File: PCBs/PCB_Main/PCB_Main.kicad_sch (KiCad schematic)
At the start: 12 parts, among them J1 Conn_01x03_Pin, J10 To_Audio, J3 Light Sensor Connector, J4 USB_B_Micro, J5 LED connectors, J6 XT60-M, J7 HUB75, U8 ESP32-WROVER-E

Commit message: new
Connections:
- net at J3.2 (Pin_2): now also U8.6 (GPIO34/ADC1_CH6)
- net at J10.1 (Pin_1): now also U8.10 (DAC_1/ADC2_CH8/GPIO25)
- net at J10.2 (Pin_2): now also U8.11 (DAC_2/ADC2_CH9/GPIO26)
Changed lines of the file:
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@@
+    (stroke (width 0) (type default))
+  )
+  (wire (pts (xy 121.92 69.85) (xy 121.92 59.69))
     (stroke (width 0) (type default))
   )
@@
   )
   (wire (pts (xy 25.4 15.24) (xy 25.4 19.05))
+    (stroke (width 0) (type default))
+  )
+  (wire (pts (xy 208.28 64.77) (xy 262.89 64.77))
+    (stroke (width 0) (type default))
+  )
+  (wire (pts (xy 121.92 59.69) (xy 137.16 59.69))
+    (stroke (width 0) (type default))
+  )
+  (wire (pts (xy 101.6 69.85) (xy 121.92 69.85))
+    (stroke (width 0) (type default))
+  )
+  (wire (pts (xy 260.35 67.31) (xy 260.35 77.47))
     (stroke (width 0) (type default))
   )
@@
     (stroke (width 0) (type default))
   )
+  (wire (pts (xy 262.89 64.77) (xy 262.89 74.93))
+    (stroke (width 0) (type default))
+  )
+  (wire (pts (xy 262.89 74.93) (xy 266.7 74.93))
+    (stroke (width 0) (type default))
+  )
+  (wire (pts (xy 260.35 77.47) (xy 266.7 77.47))
+    (stroke (width 0) (type default))
+  )
   (wire (pts (xy 262.89 25.4) (xy 265.43 25.4))
     (stroke (width 0) (type default))
@@
   )
   (wire (pts (xy 262.89 43.18) (xy 262.89 49.53))
+    (stroke (width 0) (type default))
+  )
+  (wire (pts (xy 101.6 39.37) (xy 101.6 69.85))
     (stroke (width 0) (type default))
   )
@@
     (stroke (width 0) (type default))
   )
+  (wire (pts (xy 109.22 39.37) (xy 101.6 39.37))
+    (stroke (width 0) (type default))
+  )
+  (wire (pts (xy 208.28 67.31) (xy 260.35 67.31))
+    (stroke (width 0) (type default))
+  )

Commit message: updated PCB main
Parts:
- removed J10: To_Audio, Connector_JST:JST_EH_B2B-EH-A_1x02_P2.50mm_Vertical, symbol Connector_Generic:Conn_01x02
- removed J3: Light Sensor Connector, Connector_JST:JST_EH_B3B-EH-A_1x03_P2.50mm_Vertical, symbol Connector_Generic:Conn_01x03
- removed U8: ESP32-WROVER-E, PCM_Espressif:ESP32-WROVER-E, symbol PCM_Espressif:ESP32-WROVER-E
- removed VR1: 5V-3.3V LDO, Artisyn_Components:VREG_LM3940IMP-3.3_NOPB, symbol LM3940IMP-3.3_NOPB:LM3940IMP-3.3_NOPB
- added C1, C2, C8: 22uF, Capacitor_SMD:C_0805_2012Metric, symbol Device:C
- added C3: 4.7uF, Capacitor_SMD:C_0805_2012Metric, symbol Device:C
- added C4, C5, C6, C7, C9: .1uF, Capacitor_SMD:C_0805_2012Metric, symbol Device:C
- added D1: RED LED, symbol Device:LED
- added D2, D3, D4, D5: BZX84Cxx, Package_TO_SOT_SMD:SOT-23, symbol Diode:BZX84Cxx
- added J2: To_Audio, Connector_PinHeader_2.54mm:PinHeader_1x02_P2.54mm_Vertical, symbol Connector:Conn_01x02_Pin
- added LightSensorConnector1: Conn_01x03_Pin, Connector_PinHeader_2.54mm:PinHeader_1x03_P2.54mm_Vertical, symbol Connector:Conn_01x03_Pin
- added Q1, Q2: S8050, Package_TO_SOT_THT:TO-92_Inline, symbol Transistor_BJT:S8050
- added R1: 22.1k, Resistor_SMD:R_0805_2012Metric, symbol Device:R
- added R10, R5: 2k, Resistor_SMD:R_0805_2012Metric, symbol Device:R
- added R11, R12, R14: 100, Resistor_SMD:R_0805_2012Metric, symbol Device:R
- added R13, R6, R7, R8: 10k, Resistor_SMD:R_0805_2012Metric, symbol Device:R
- added R2: 47.5k, Resistor_SMD:R_0805_2012Metric, symbol Device:R
- added R4, R9: 0, Resistor_SMD:R_0805_2012Metric, symbol Device:R
- added SW1, SW2: SW_Push, symbol Switch:SW_Push
- added U1: CP2102N-Axx-xQFN28, Package_DFN_QFN:QFN-28-1EP_5x5mm_P0.5mm_EP3.35x3.35mm, symbol Interface_USB:CP2102N-Axx-xQFN28
- added U2: AMS1117-3.3, Package_TO_SOT_SMD:SOT-223-3_TabPin2, symbol Regulator_Linear:AMS1117-3.3
- added U3: ESP32-WROOM-E, PCM_Espressif:ESP32-WROOM-32E, symbol PCM_Espressif:ESP32-WROOM-E
- J1: value Conn_01x03_Pin -> LED Connectors+
- J5: value LED connectors -> LED connectors -
- J7: footprint (none) -> Connector_PinHeader_2.54mm:PinHeader_2x08_P2.54mm_Vertical
- R3, TH1: footprint (none) -> Resistor_SMD:R_0805_2012Metric
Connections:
- net GND: now also C1.2, C2.2, C3.1, C4.1, C5.1, C6.1, C7.2, C8.2, C9.2, D1.1 (K), D2.1 (A), D4.1 (A), D5.1 (A), LightSensorConnector1.1 (Pin_1), R2.2, R6.2, SW1.1, SW2.1, U1.29 (GND), U1.3 (GND), U2.1 (GND), U3.1 (GND), U3.15 (GND), U3.38 (GND), U3.39 (GND_THERMAL)
- net VCC: now also C1.1, D3.3 (K), R10.1, U2.3 (VI); no longer J4.1 (VBUS)
- net 3.3V: now reaches TH1.1
- net 3.3V: now also C2.1, C3.2, C4.2, C8.1, C9.1, LightSensorConnector1.3 (Pin_3), R13.1, R5.1, U1.6 (VDD), U1.7 (VREGIN), U2.2 (VO), U3.2 (3V3)
- net Therm_out: now reaches R3.1, TH1.2
- net at J4.2 (D-): now also R12.1
- net at J4.3 (D+): now also R11.1
- new net: R1.1, R2.1, U1.8 (VBUS)
- new net: R5.2, U1.9 (~{RST})
- new net: R6.1, U1.11 (~{SUSPEND})
- new net: Q2.2 (B), R8.2
- new net: D1.2 (A), R10.2
- new net: Q1.2 (B), R7.2
- new net: J4.1 (VBUS), R14.1
- new net: C7.1, R13.2
- new net CTS: U1.23 (~{CTS})
- new net DCD: U1.1 (~{DCD})
- new net DSR: U1.27 (~{DSR})
- new net DTR: Q2.1 (E), R7.1, U1.28 (~{DTR})
- new net EN: C6.2, Q1.3 (C), SW2.2
- new net IO0: C5.2, Q2.3 (C), SW1.2
- new net Light_Out: LightSensorConnector1.2 (Pin_2)
- new net RI: U1.2 (~{RI}/CLK)
- new net RTS: Q1.1 (E), R8.1, U1.24 (~{RTS})
- new net RXD: R9.2, U1.25 (RXD)
- new net RXD0: R4.1
- new net TXD: R4.2, U1.26 (TXD)
- new net TXD0: R9.1
- new net USB_DN: D5.3 (K), R11.2, U1.5 (D-)
- new net USB_DP: D4.3 (K), R12.2, U1.4 (D+)
- new net Vbus: D2.3 (K), D3.1 (A), R1.2, R14.2
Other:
- note added: "5V-3.3VLDO"
- note added: "Audio Signals to other board"
- note added: "Exterior Bluetooth module"
- note added: "LED CONNECTORS"
- note added: "LED Display Signals"
- note added: "MICRO USB 5V USB-UART"
- note added: "MIRCO"
- note added: "POWER ONTO BOARD"
- note added: "SENSORS"
- note added: "SWITCH BUTTIONS"
- moved on the sheet: HM19, J1, J4, J5, J6, J7, R3, TH1

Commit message: latest PCBs
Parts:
- added C10: 22uF, Capacitor_SMD:C_0805_2012Metric, symbol Device:C
- added C11, C12: .1uF, Capacitor_SMD:C_0805_2012Metric, symbol Device:C
- added R15: 10k, Resistor_SMD:R_0805_2012Metric, symbol Device:R
- added U4: PCM5102A, Package_SO:TSSOP-20_4.4x6.5mm_P0.65mm, symbol Audio:PCM5102A
- added U6: ESP32-WROVER-E, PCM_Espressif:ESP32-WROVER-E, symbol PCM_Espressif:ESP32-WROVER-E
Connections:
- net 3.3V: now also C10.1, C11.1, R15.1, U6.2 (3V3)
- net GND: now also C10.2, C11.2, C12.2, U6.1 (GND), U6.15 (GND), U6.38 (GND), U6.39 (GND_THERMAL)
- new net: C12.1, R15.2
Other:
- note added: "External DAC"
- note added: "MIRCO1 WROOM"
- note added: "MIRCO1 WROVER"
- note removed: "MIRCO"

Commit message: PCB combination
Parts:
- removed J2: To_Audio, Connector_PinHeader_2.54mm:PinHeader_1x02_P2.54mm_Vertical, symbol Connector:Conn_01x02_Pin
- added C0L1, C0R1, C3b1: 1000uF, Artisyn_Components:Audio_1000uF, symbol Device:C_Polarized_US
- added Cb1: 100uF, Artisyn_Components:Audio_100uF, symbol Device:C_Polarized_US
- added Cbst1, Cres1, Cvin1: 470.0 nF, Capacitor_SMD:C_0805_2012Metric, symbol Device:C
- added Ccomp1: 18.0 nF, Capacitor_SMD:C_1812_4532Metric, symbol Device:C
- added Ccomp2: 1.0 nF, Capacitor_SMD:C_0805_2012Metric, symbol Device:C
- added CiL1, CiR1, Csc1, CsnL1, CsnR1: .1uF, Capacitor_SMD:C_0805_2012Metric, symbol Device:C
- added Cin1: 270uF, Artisyn_Components:PCAP_SVP_E7_PAN, symbol Device:C_Polarized_US
- added Cout1: 560.0 uF, Artisyn_Components:PCAP_SVP_F12_PAN, symbol Device:C_Polarized_US
- added Coutx1: 47.0 uF, Capacitor_SMD:C_1206_3216Metric, symbol Device:C
- added Css1: 33.0 nF, Capacitor_SMD:C_0805_2012Metric, symbol Device:C
- added Cvcc1: 10.0 uF, Capacitor_SMD:C_0805_2012Metric, symbol Device:C
- added Dbst1: D_Schottky, Diode_SMD:D_SMA, symbol Device:D_Schottky
- added J10: To_Speaker_R, Connector_PinHeader_2.54mm:PinHeader_1x02_P2.54mm_Vertical, symbol Connector_Generic:Conn_01x02
- added J9: To_Speaker_L, Connector_PinHeader_2.54mm:PinHeader_1x02_P2.54mm_Vertical, symbol Connector_Generic:Conn_01x02
- added L1: 3.3 µH, Artisyn_Components:IND_R3-R_EAT, symbol Device:L
- added M1: CSD17581Q3, Artisyn_Components:CSD17309Q3, symbol Custom_Lib:CSD17309Q3
- added M2: CSD17581Q3A, Artisyn_Components:CSD17309Q3A, symbol CSD17581Q3A:CSD17581Q3A
- added Rcomp1: 23.7k, Resistor_SMD:R_0805_2012Metric, symbol Device:R
- added Rfbb1: 3.65k, Resistor_SMD:R_0805_2012Metric, symbol Device:R
- added Rfbt1: 39.0k, Resistor_SMD:R_0805_2012Metric, symbol Device:R
- added Rsense1: 1.5m, Resistor_SMD:R_2512_6332Metric, symbol Device:R
- added Rslope1: 150.0k, Resistor_SMD:R_0805_2012Metric, symbol Device:R
- added RsnL1, RsnR1: 2.7, Resistor_SMD:R_0805_2012Metric, symbol Device:R
- added Rt1: 41.2k, Resistor_SMD:R_0805_2012Metric, symbol Device:R
- added Ruvb1: 19.1k, Resistor_SMD:R_0805_2012Metric, symbol Device:R
- added Ruvt1: 49.9k, Resistor_SMD:R_0805_2012Metric, symbol Device:R
- added Rvin1: 3.01, Resistor_SMD:R_1206_3216Metric, symbol Device:R
- added U5: LM5122MH/NOPB, Artisyn_Components:LM512220A_L, symbol LM5122:LM5122MH_NOPB
- added U7: LM4752TS, Artisyn_Components:LM4752, symbol LM4752TS:LM4752TS
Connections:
- net GND: now also C3b1.2, Cb1.2, Cin1.2, Cout1.2, Coutx1.2, Cres1.2, CsnL1.2, CsnR1.2, Css1.2, Cvcc1.1, Cvin1.2, J10.2 (Pin_2), J9.2 (Pin_2), M1.1 (S1), M1.2 (S2), M1.3 (S3), Rfbb1.2, Rslope1.2, Rt1.2, Ruvb1.2, U5.13 (MODE), U5.15 (PGND), U5.2 (OPT), U5.9 (AGND), U7.4 (GND)
- net VCC: now also Cin1.1, Rsense1.2, Ruvt1.1, Rvin1.1, U5.4 (CSP)
- new net: CiL1.2, U7.2 (In_B)
- new net: Cvcc1.2, Dbst1.2 (A), U5.17 (VCC)
- new net: Ccomp2.1, Rcomp1.1, U5.11 (COMP)
- new net: Ccomp1.2, Ccomp2.2, Rfbb1.1, Rfbt1.2, U5.10 (FB)
- new net: Cout1.1, Coutx1.1, Csc1.1, M2.5 (DRAIN), M2.6 (DRAIN), M2.7 (DRAIN), M2.8 (DRAIN), M2.9 (DRAIN), Rfbt1.1, U7.3 (Vcc)
- new net: C0R1.1, RsnR1.1, U7.7 (Out_A)
- new net: C0R1.2, J10.1 (Pin_1)
- new net: C0L1.1, RsnL1.1, U7.1 (Out_B)
- new net: CsnL1.1, RsnL1.2
- new net: Cb1.1, U7.5 (Bias)
- new net: CiR1.2, U7.6 (In_A)
- new net: C3b1.1, Csc1.2
- new net: Ccomp1.1, Rcomp1.2
- new net: Rt1.1, U5.8 (SYNCIN_RT)
- new net: Cbst1.2, L1.2, M1.5 (D1), M1.6 (D2), M1.7 (D3), M1.8 (D4), M2.1 (SOURCE), M2.2 (SOURCE), M2.3 (SOURCE), U5.18 (SW)
- new net: M2.4 (GATE), U5.19 (HO)
- new net: Cvin1.1, Rvin1.2, U5.5 (VIN)
- new net: Rslope1.1, U5.12 (SLOPE)
- new net: L1.1, Rsense1.1, U5.3 (CSN)
- new net: CsnR1.1, RsnR1.2
- new net: Ruvb1.1, Ruvt1.2, U5.6 (UVLO)
- new net: C0L1.2, J9.1 (Pin_1)
- new net: Css1.1, U5.7 (SS)
- new net: Cres1.1, U5.14 (RES)
- new net: M1.4 (G), U5.16 (LO)
- new net: Cbst1.1, Dbst1.1 (K), U5.20 (BST)
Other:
- note added: "Boost and Audio Converter"
- note removed: "Audio Signals to other board"

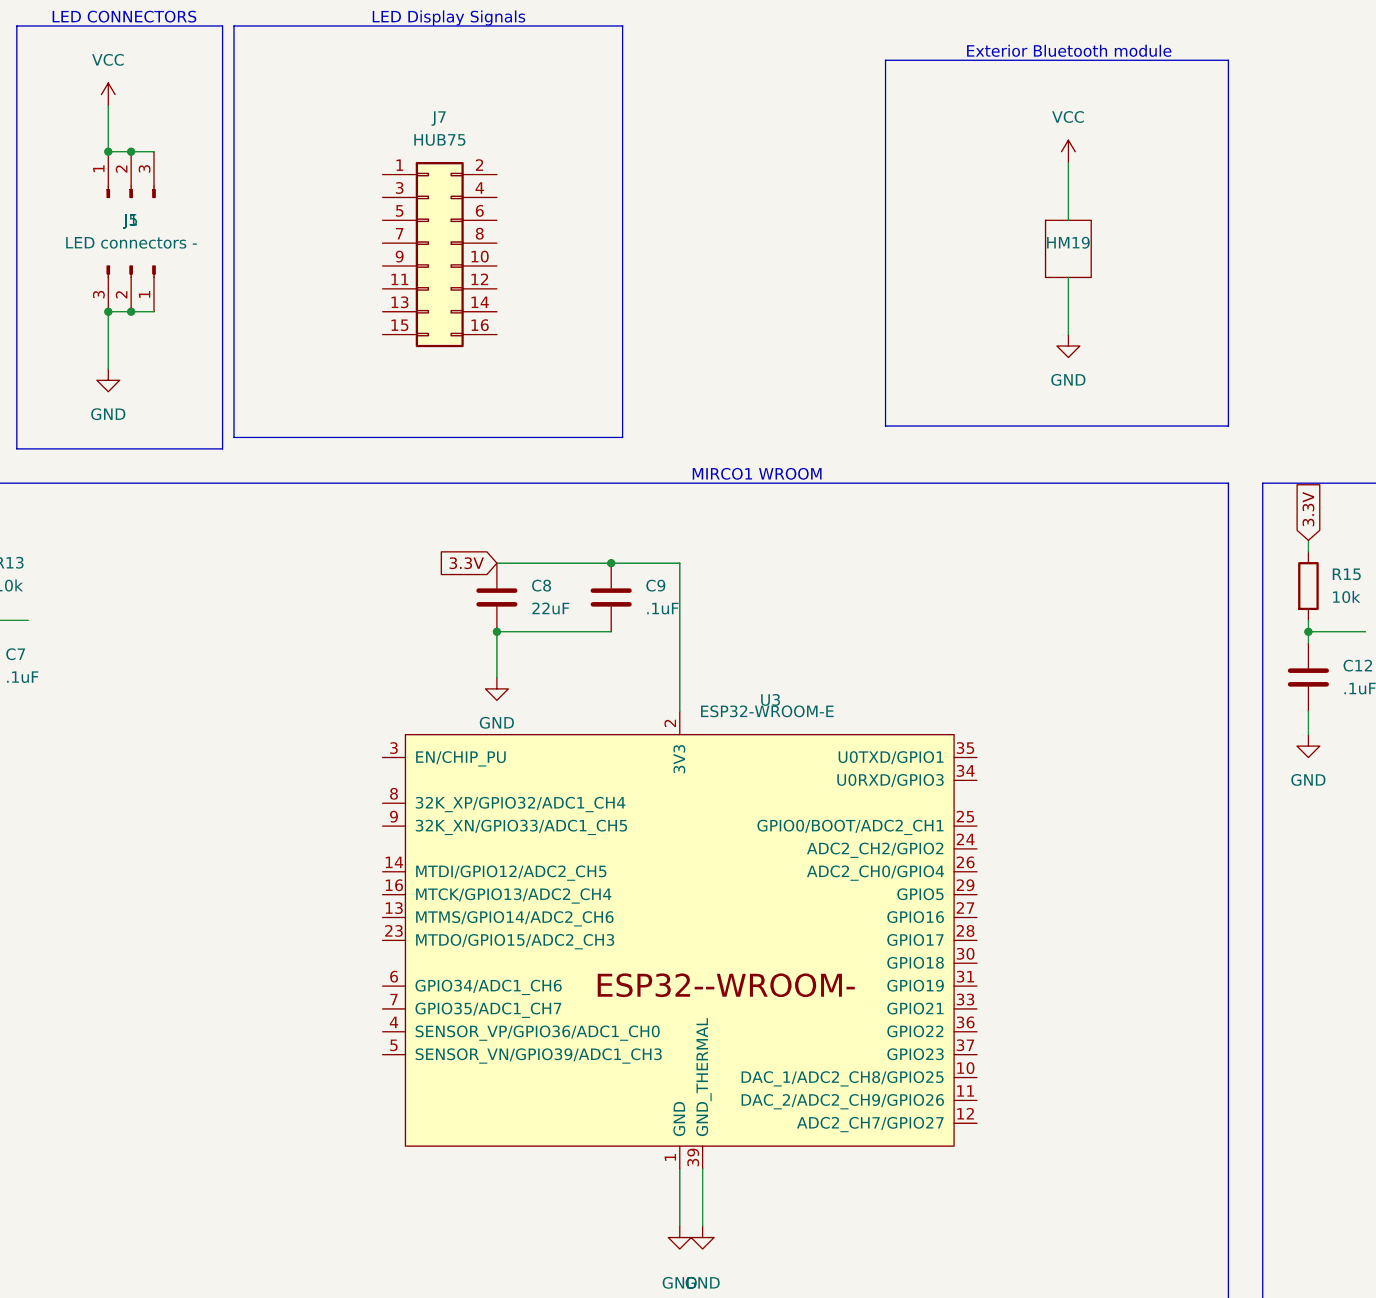
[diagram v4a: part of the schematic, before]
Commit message: PCB, LED pins and light sensor pins added
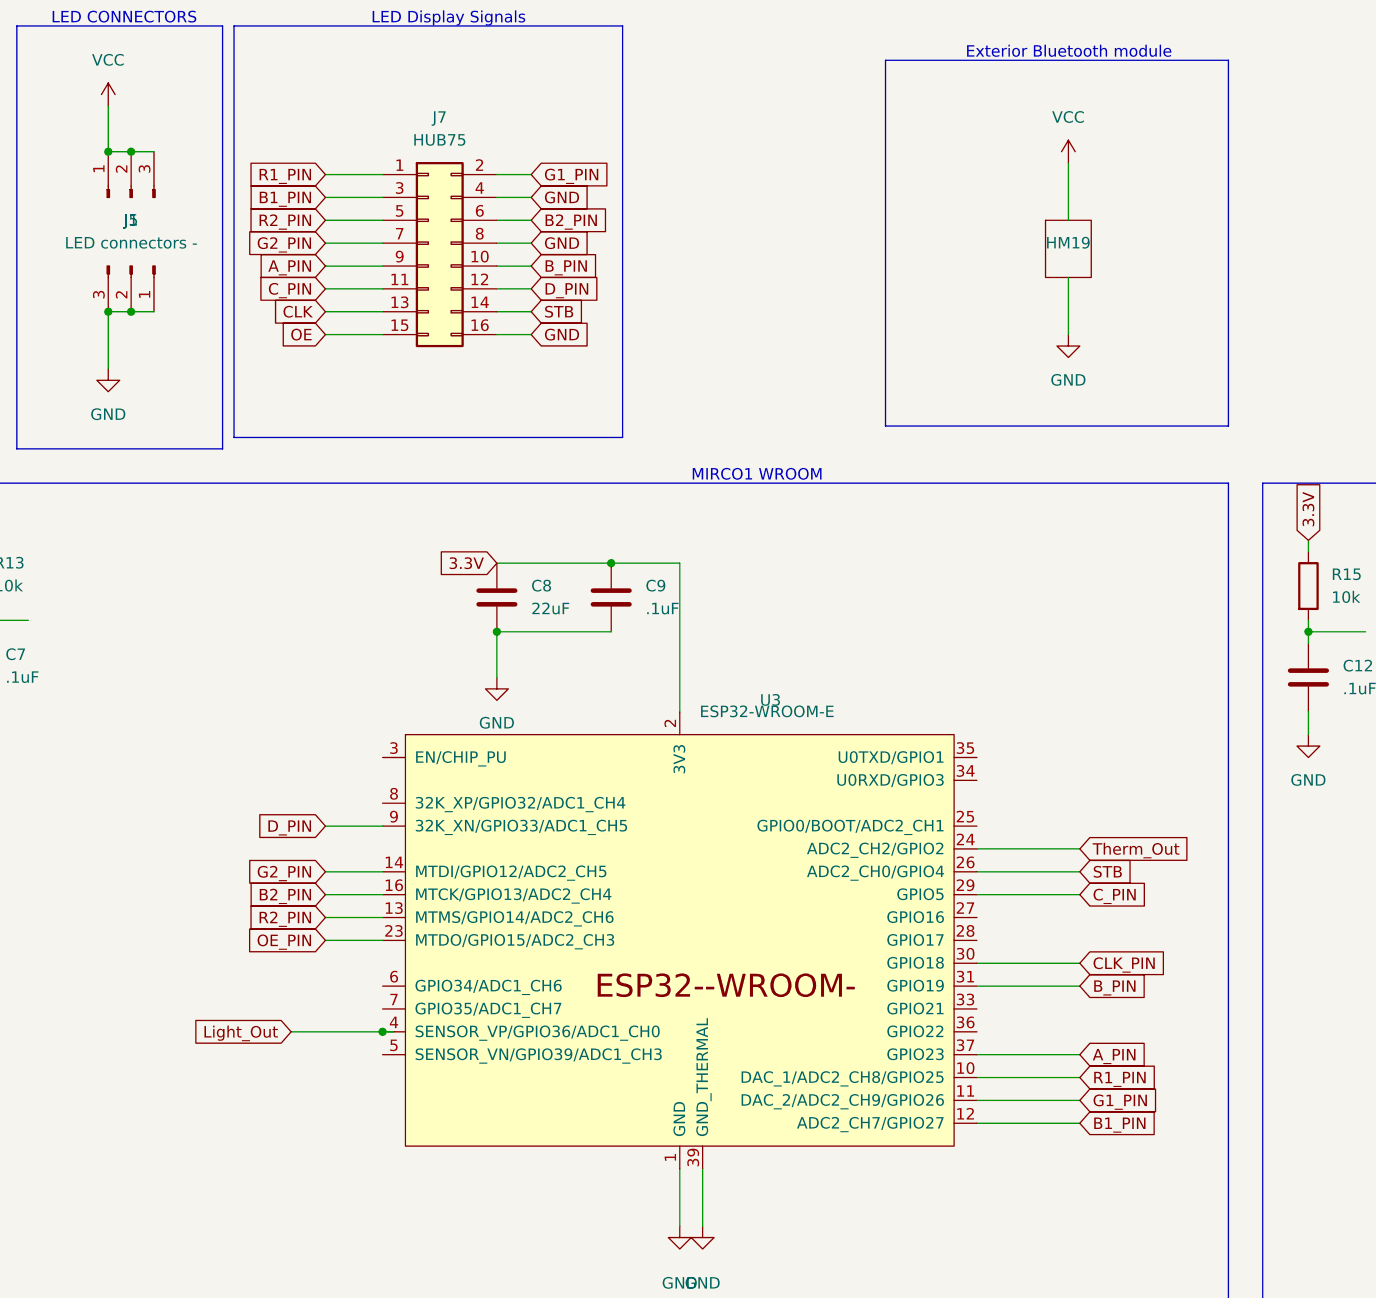
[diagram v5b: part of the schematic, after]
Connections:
- net GND: now also J7.16 (Pin_16), J7.4 (Pin_4), J7.8 (Pin_8)
- net Light_Out: now also U3.4 (SENSOR_VP/GPIO36/ADC1_CH0)
- net R1_PIN: now reaches U3.10 (DAC_1/ADC2_CH8/GPIO25)
- net R1_PIN: now also J7.1 (Pin_1)
- net G1_PIN: now reaches U3.11 (DAC_2/ADC2_CH9/GPIO26)
- net G1_PIN: now also J7.2 (Pin_2)
- net B1_PIN: now reaches U3.12 (ADC2_CH7/GPIO27)
- net B1_PIN: now also J7.3 (Pin_3)
- net R2_PIN: now reaches U3.13 (MTMS/GPIO14/ADC2_CH6)
- net R2_PIN: now also J7.5 (Pin_5)
- net G2_PIN: now reaches U3.14 (MTDI/GPIO12/ADC2_CH5)
- net G2_PIN: now also J7.7 (Pin_7)
- net B2_PIN: now reaches U3.16 (MTCK/GPIO13/ADC2_CH4)
- net B2_PIN: now also J7.6 (Pin_6)
- net OE_PIN: now reaches U3.23 (MTDO/GPIO15/ADC2_CH3)
- net Therm_Out: now reaches U3.24 (ADC2_CH2/GPIO2)
- net STB: now reaches U3.26 (ADC2_CH0/GPIO4)
- net STB: now also J7.14 (Pin_14)
- net C_PIN: now reaches U3.29 (GPIO5)
- net C_PIN: now also J7.11 (Pin_11)
- net CLK_PIN: now reaches U3.30 (GPIO18)
- net B_PIN: now reaches U3.31 (GPIO19)
- net B_PIN: now also J7.10 (Pin_10)
- net A_PIN: now reaches U3.37 (GPIO23)
- net A_PIN: now also J7.9 (Pin_9)
- net D_PIN: now reaches U3.9 (32K_XN/GPIO33/ADC1_CH5)
- net D_PIN: now also J7.12 (Pin_12)
- net CLK: now reaches J7.13 (Pin_13)
- net OE: now reaches J7.15 (Pin_15)

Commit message: UART pins
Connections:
- net WROOMRX: now reaches U3.27 (GPIO16)
- net WROOMRX: now also U6.12 (ADC2_CH7/GPIO27)
- net WROOMTX: now reaches U3.28 (GPIO17)
- net WROOMTX: now also U6.13 (MTMS/GPIO14/ADC2_CH6)
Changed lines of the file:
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@@
+    (stroke (width 0) (type default))
+  )
+  (wire (pts (xy 321.31 107.95) (xy 328.93 107.95))
     (stroke (width 0) (type default))
   )
@@
     (stroke (width 0) (type default))
   )
+  (wire (pts (xy 256.54 104.14) (xy 267.97 104.14))
+    (stroke (width 0) (type default))
+  )
   (wire (pts (xy 41.91 120.65) (xy 41.91 121.92))
     (stroke (width 0) (type default))
@@
     (stroke (width 0) (type default))
   )
+  (wire (pts (xy 256.54 106.68) (xy 267.97 106.68))
+    (stroke (width 0) (type default))
+  )
   (wire (pts (xy 115.57 102.87) (xy 121.92 102.87))
     (stroke (width 0) (type default))
@@
   )
   (wire (pts (xy 256.54 99.06) (xy 267.97 99.06))
+    (stroke (width 0) (type default))
+  )
+  (wire (pts (xy 400.05 125.73) (xy 407.67 125.73))
     (stroke (width 0) (type default))
   )
@@
     )
   )
+  (global_label "WROOMTX" (shape input) (at 267.97 106.68 0) (fields_autoplaced)
+    (effects (font (size 1.27 1.27)) (justify left))
+    (property "Intersheetrefs" "${INTERSHEET_REFS}" (at 279.9661 106.68 0)
+      (effects (font (size 1.27 1.27)) (justify left) hide)
+    )
+  )
   (global_label "DTR" (shape input) (at 19.05 127 180) (fields_autoplaced)
     (effects (font (size 1.27 1.27)) (justify right))
@@
     )
   )
+  (global_label "WROOMRX" (shape input) (at 407.67 125.73 0) (fields_autoplaced)
+    (effects (font (size 1.27 1.27)) (justify left))
+    (property "Intersheetrefs" "${INTERSHEET_REFS}" (at 419.9685 125.73 0)
+      (effects (font (size 1.27 1.27)) (justify left) hide)
+    )
+  )
   (global_label "IO0" (shape input) (at 40.64 173.99 0) (fields_autoplaced)
     (effects (font (size 1.27 1.27)) (justify left))
@@
     )
   )
+  (global_label "WROOMTX" (shape input) (at 321.31 107.95 180) (fields_autoplaced)
+    (effects (font (size 1.27 1.27)) (justify right))
+    (property "Intersheetrefs" "${INTERSHEET_REFS}" (at 309.3139 107.95 0)
+      (effects (font (size 1.27 1.27)) (justify right) hide)
+    )
+  )
   (global_label "USB_DN" (shape input) (at 90.17 100.33 180) (fields_autoplaced)
     (effects (font (size 1.27 1.27)) (justify right))
@@
     )
   )
+  (global_label "WROOMRX" (shape input) (at 267.97 104.14 0) (fields_autoplaced)
+    (effects (font (size 1.27 1.27)) (justify left))
+    (property "Intersheetrefs" "${INTERSHEET_REFS}" (at 280.2685 104.14 0)
+      (effects (font (size 1.27 1.27)) (justify left) hide)
+    )
+  )
